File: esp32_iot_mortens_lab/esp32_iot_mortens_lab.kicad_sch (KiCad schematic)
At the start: 27 parts, among them J1 Conn_01x04, J2 Screw_Terminal_01x03, J3 Screw_Terminal_01x08, J4 Screw_Terminal_01x02, J5 USB_C_Receptacle_USB2.0_16P, K1 RT314A05, Q1 UMH3N, Q2 BC817, SW1 SW_Push, U1 ESP32-WROOM-32D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

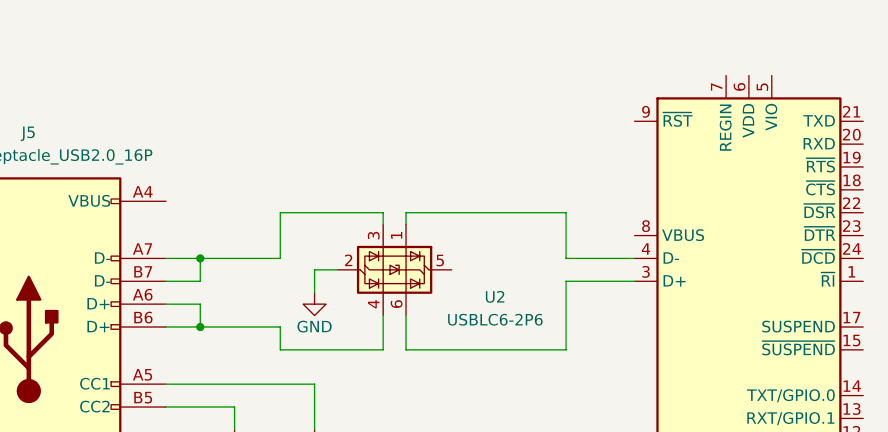
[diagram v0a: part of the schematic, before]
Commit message: upto adding power to the usb/uart circuit
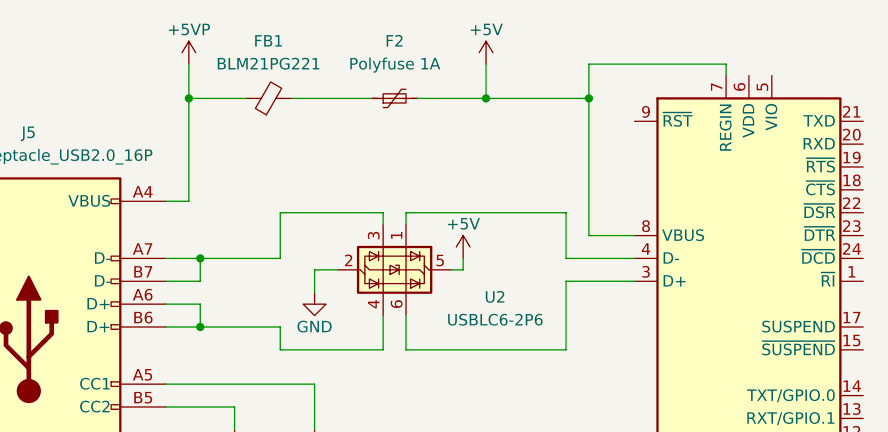
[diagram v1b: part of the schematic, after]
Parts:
- added F2: Polyfuse 1A, symbol Device:Polyfuse_Small
- added FB1: BLM21PG221, symbol Device:FerriteBead_Small
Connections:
- net +5V: now reaches U2.5 (VBUS)
- net +5V: now also U3.7 (REGIN), U3.8 (VBUS), F2.2
- net +5VP: now reaches J5.A4 (VBUS), J5.A9 (VBUS), J5.B4 (VBUS), J5.B9 (VBUS)
- net +5VP: now also FB1.1
- new net: F2.1, FB1.2

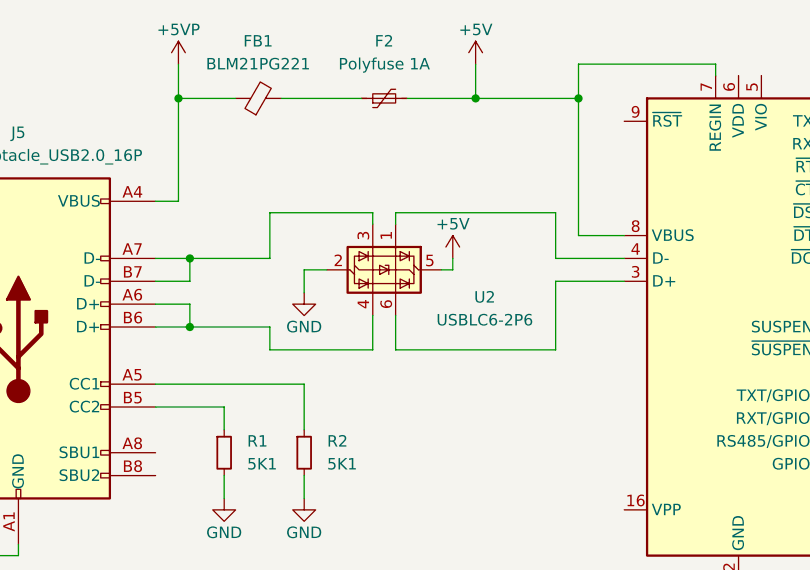
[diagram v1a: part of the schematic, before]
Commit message: pins 1,6 to D+; pins 3,4 to D- as per GPT and datasheet
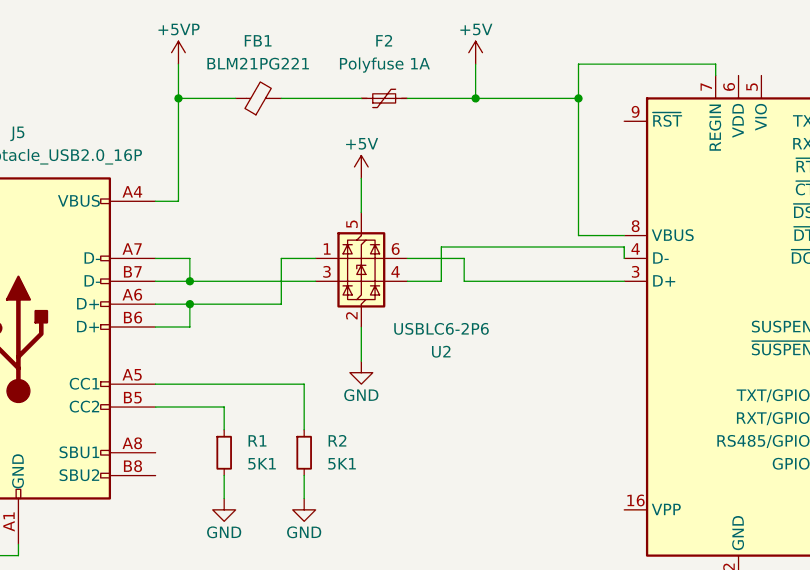
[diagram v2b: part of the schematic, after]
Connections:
- net at U2.1 (I/O1): now also J5.A6 (D+), J5.B6 (D+); no longer U3.4 (D-)
- new net: U2.4 (I/O2), U3.4 (D-)
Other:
- moved on the sheet: U2
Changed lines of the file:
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@@
+	)
+	(junction
+		(at 58.42 62.23)
+		(diameter 0)
+		(color 0 0 0 0)
 	)
 	(junction
@@
 	)
 	(junction
-		(at 101.6 41.91)
+		(at 58.42 64.77)
 		(diameter 0)
 		(color 0 0 0 0)
 	)
 	(junction
-		(at 58.42 67.31)
-		(diameter 0)
-		(color 0 0 0 0)
-	)
-	(junction
-		(at 58.42 59.69)
+		(at 101.6 41.91)
 		(diameter 0)
 		(color 0 0 0 0)
@@
 	(wire
 		(pts
-			(xy 71.12 60.96) (xy 73.66 60.96)
-		)
-		(stroke
-			(width 0)
-			(type default)
-		)
-	)
-	(wire
-		(pts
-			(xy 67.31 69.85) (xy 67.31 67.31)
+			(xy 82.55 62.23) (xy 86.36 62.23)
+		)
+		(stroke
+			(width 0)
+			(type default)
+		)
+	)
+	(wire
+		(pts
+			(xy 77.47 50.8) (xy 77.47 54.61)
 		)
 		(stroke
@@
 	(wire
 		(pts
-			(xy 81.28 54.61) (xy 99.06 54.61)
+			(xy 77.47 67.31) (xy 77.47 71.12)
 		)
 		(stroke
@@
 	(wire
 		(pts
-			(xy 99.06 62.23) (xy 106.68 62.23)
+			(xy 72.39 59.69) (xy 68.58 59.69)
 		)
 		(stroke
@@
 	(wire
 		(pts
+			(xy 88.9 62.23) (xy 106.68 62.23)
+		)
+		(stroke
+			(width 0)
+			(type default)
+		)
+	)
+	(wire
+		(pts
 			(xy 39.37 91.44) (xy 39.37 92.71)
 		)
@@
 	(wire
 		(pts
-			(xy 81.28 66.04) (xy 81.28 69.85)
-		)
-		(stroke
-			(width 0)
-			(type default)
-		)
-	)
-	(wire
-		(pts
 			(xy 57.15 38.1) (xy 57.15 41.91)
 		)
@@
 	(wire
 		(pts
-			(xy 67.31 69.85) (xy 78.74 69.85)
-		)
-		(stroke
-			(width 0)
-			(type default)
-		)
-	)
-	(wire
-		(pts
-			(xy 67.31 59.69) (xy 58.42 59.69)
+			(xy 68.58 59.69) (xy 68.58 64.77)
+		)
+		(stroke
+			(width 0)
+			(type default)
+		)
+	)
+	(wire
+		(pts
+			(xy 58.42 62.23) (xy 72.39 62.23)
 		)
 		(stroke
@@
 	(wire
 		(pts
-			(xy 81.28 55.88) (xy 81.28 54.61)
-		)
-		(stroke
-			(width 0)
-			(type default)
-		)
-	)
-	(wire
-		(pts
-			(xy 67.31 54.61) (xy 78.74 54.61)
+			(xy 88.9 59.69) (xy 88.9 62.23)
 		)
 		(stroke
@@
 	(wire
 		(pts
-			(xy 87.63 60.96) (xy 87.63 59.69)
-		)
-		(stroke
-			(width 0)
-			(type default)
-		)
-	)
-	(wire
-		(pts
 			(xy 101.6 38.1) (xy 116.84 38.1)
 		)
@@
 	(wire
 		(pts
-			(xy 78.74 54.61) (xy 78.74 55.88)
-		)
-		(stroke
-			(width 0)
-			(type default)
-		)
-	)
-	(wire
-		(pts
-			(xy 81.28 69.85) (xy 99.06 69.85)
-		)
-		(stroke
-			(width 0)
-			(type default)
-		)
-	)
-	(wire
-		(pts
-			(xy 67.31 59.69) (xy 67.31 54.61)
+			(xy 86.36 62.23) (xy 86.36 58.42)
 		)
 		(stroke
@@
 	(wire
 		(pts
-			(xy 58.42 67.31) (xy 58.42 64.77)
+			(xy 58.42 64.77) (xy 58.42 67.31)
 		)
 		(stroke
@@
 	(wire
 		(pts
-			(xy 78.74 66.04) (xy 78.74 69.85)
-		)
-		(stroke
-			(width 0)
-			(type default)
-		)
-	)
-	(wire
-		(pts
-			(xy 99.06 69.85) (xy 99.06 62.23)
-		)
-		(stroke
-			(width 0)
-			(type default)
-		)
-	)
-	(wire
-		(pts
-			(xy 86.36 60.96) (xy 87.63 60.96)
+			(xy 58.42 59.69) (xy 58.42 62.23)
 		)
 		(stroke
@@
 	(wire
 		(pts
-			(xy 67.31 67.31) (xy 58.42 67.31)
-		)
-		(stroke
-			(width 0)
-			(type default)
-		)
-	)
-	(wire
-		(pts
 			(xy 57.15 53.34) (xy 54.61 53.34)
 		)
@@
 	(wire
 		(pts
-			(xy 99.06 59.69) (xy 106.68 59.69)
-		)
-		(stroke
-			(width 0)
-			(type default)
-		)
-	)
-	(wire
-		(pts
 			(xy 54.61 64.77) (xy 58.42 64.77)
 		)
@@
 	(wire
 		(pts
-			(xy 71.12 63.5) (xy 71.12 60.96)
+			(xy 82.55 59.69) (xy 88.9 59.69)
 		)
 		(stroke
@@
 	(wire
 		(pts
-			(xy 99.06 54.61) (xy 99.06 59.69)
+			(xy 68.58 64.77) (xy 58.42 64.77)
+		)
+		(stroke
+			(width 0)
+			(type default)
+		)
+	)
+	(wire
+		(pts
+			(xy 86.36 58.42) (xy 106.68 58.42)
 		)
 		(stroke
@@
 	(wire
 		(pts
-			(xy 58.42 62.23) (xy 58.42 59.69)
+			(xy 106.68 58.42) (xy 106.68 59.69)
 		)
 		(stroke
@@
 	(symbol
 		(lib_id "Power_Protection:USBLC6-2P6")
-		(at 81.28 60.96 270)
+		(at 77.47 59.69 0)
 		(unit 1)
 		(exclude_from_sim no)
@@
 		(dnp no)
 		(property "Reference" "U2"
-			(at 91.186 64.008 90)
+			(at 86.36 70.104 0)
 			(effects
 				(font
@@
 		)
 		(property "Value" "USBLC6-2P6"
-			(at 91.186 66.548 90)
+			(at 86.36 67.564 0)
 			(effects
 				(font
@@
 		)
 		(property "Footprint" "Package_TO_SOT_SMD:SOT-666"
-			(at 74.549 61.976 0)
+			(at 78.486 66.421 0)
 			(effects
 				(font
@@
 		)
 		(property "Datasheet" "https://www.st.com/resource/en/datasheet/usblc6-2.pdf"
-			(at 72.644 61.976 0)
+			(at 78.486 68.326 0)
 			(effects
 				(font
@@
 		)
 		(property "Description" "Very low capacitance ESD protection diode, 2 data-line, SOT-666"
-			(at 81.28 60.96 0)
+			(at 77.47 59.69 0)
 			(effects
 				(font
@@
 	(symbol
 		(lib_id "power:+5V")
-		(at 87.63 59.69 0)
+		(at 77.47 50.8 0)
 		(unit 1)
 		(exclude_from_sim no)
@@
 		(dnp no)
 		(property "Reference" "#PWR07"
-			(at 87.63 63.5 0)
+			(at 77.47 54.61 0)
 			(effects
 				(font
@@
 		)
 		(property "Value" "+5V"
-			(at 87.63 55.88 0)
+			(at 77.47 46.99 0)
 			(effects
 				(font
@@
 		)
 		(property "Footprint" ""
-			(at 87.63 59.69 0)
+			(at 77.47 50.8 0)
 			(effects
 				(font
@@
 		)
 		(property "Datasheet" ""
-			(at 87.63 59.69 0)
+			(at 77.47 50.8 0)
 			(effects
 				(font
@@
 		)
 		(property "Description" "Power symbol creates a global label with name \"+5V\""
-			(at 87.63 59.69 0)
+			(at 77.47 50.8 0)
 			(effects
 				(font
@@
 	(symbol
 		(lib_id "power:GND")
-		(at 71.12 63.5 0)
+		(at 77.47 71.12 0)
 		(unit 1)
 		(exclude_from_sim no)
@@
 		(dnp no)
 		(property "Reference" "#PWR04"
-			(at 71.12 69.85 0)
+			(at 77.47 77.47 0)
 			(effects
 				(font
@@
 		)
 		(property "Value" "GND"
-			(at 71.12 67.31 0)
+			(at 77.47 74.93 0)
 			(effects
 				(font
@@
 		)
 		(property "Footprint" ""
-			(at 71.12 63.5 0)
+			(at 77.47 71.12 0)
 			(effects
 				(font
@@
 		)
 		(property "Datasheet" ""
-			(at 71.12 63.5 0)
+			(at 77.47 71.12 0)
 			(effects
 				(font
@@
 		)
 		(property "Description" "Power symbol creates a global label with name \"GND\" , ground"
-			(at 71.12 63.5 0)
-			(effects
-				(font
+			(at 77.47 71.12 0)
+			(effects
+				(font

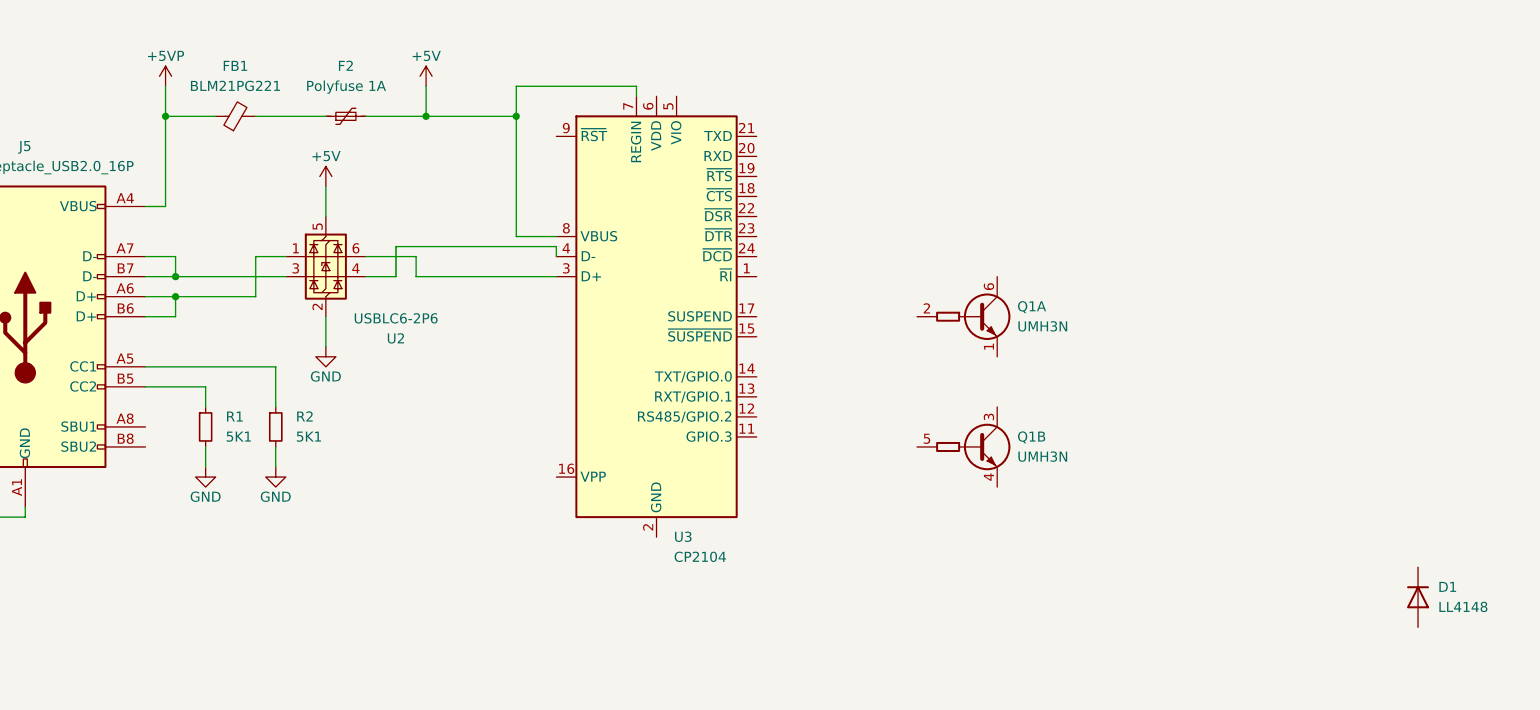
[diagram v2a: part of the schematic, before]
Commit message: added capacitors
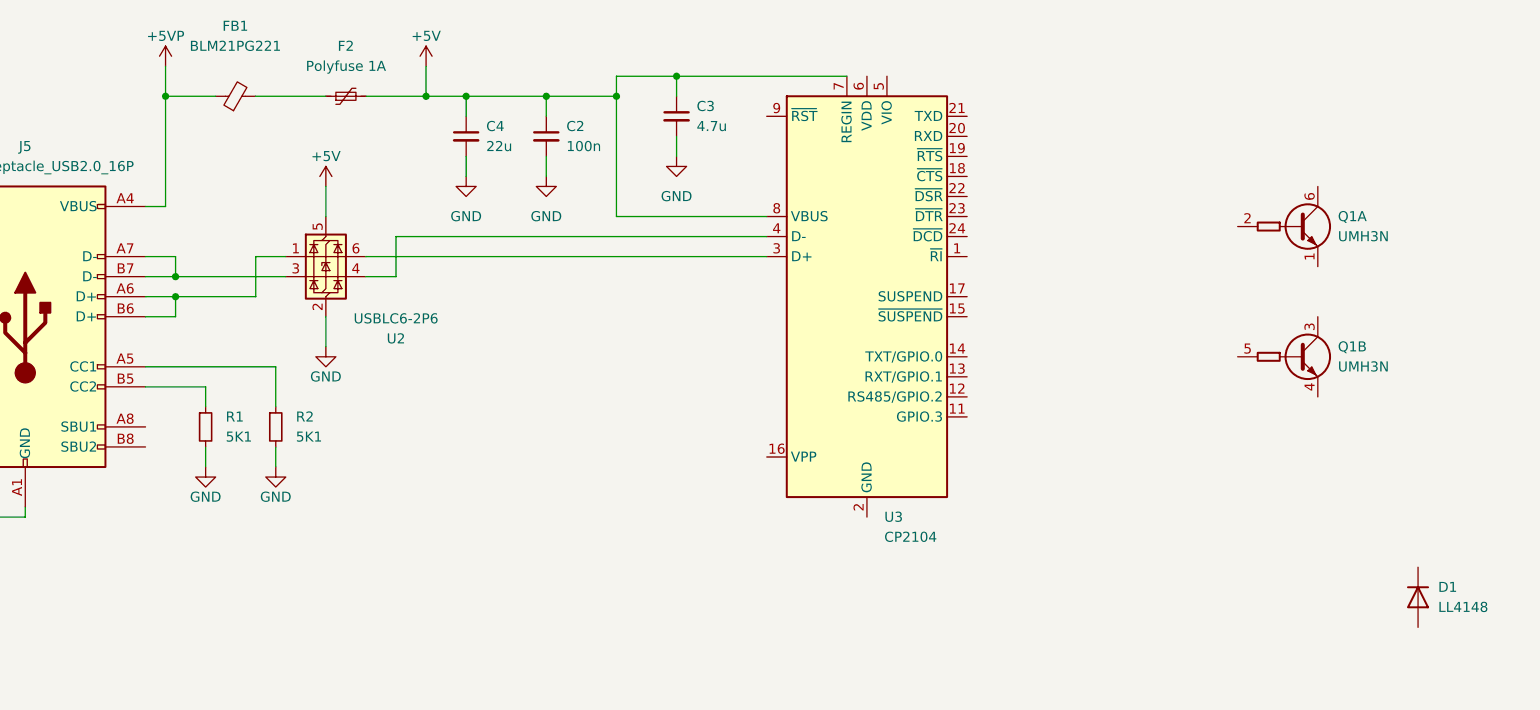
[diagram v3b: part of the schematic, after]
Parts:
- added C2: 100n, symbol Device:C_Small
- added C3: 4.7u, symbol Device:C_Small
- added C4: 22u, symbol Device:C_Small
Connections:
- net +5V: now also C2.1, C3.1, C4.1
- net GND: now also C2.2, C3.2, C4.2
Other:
- moved on the sheet: F2, FB1, Q1A, Q1B, U3

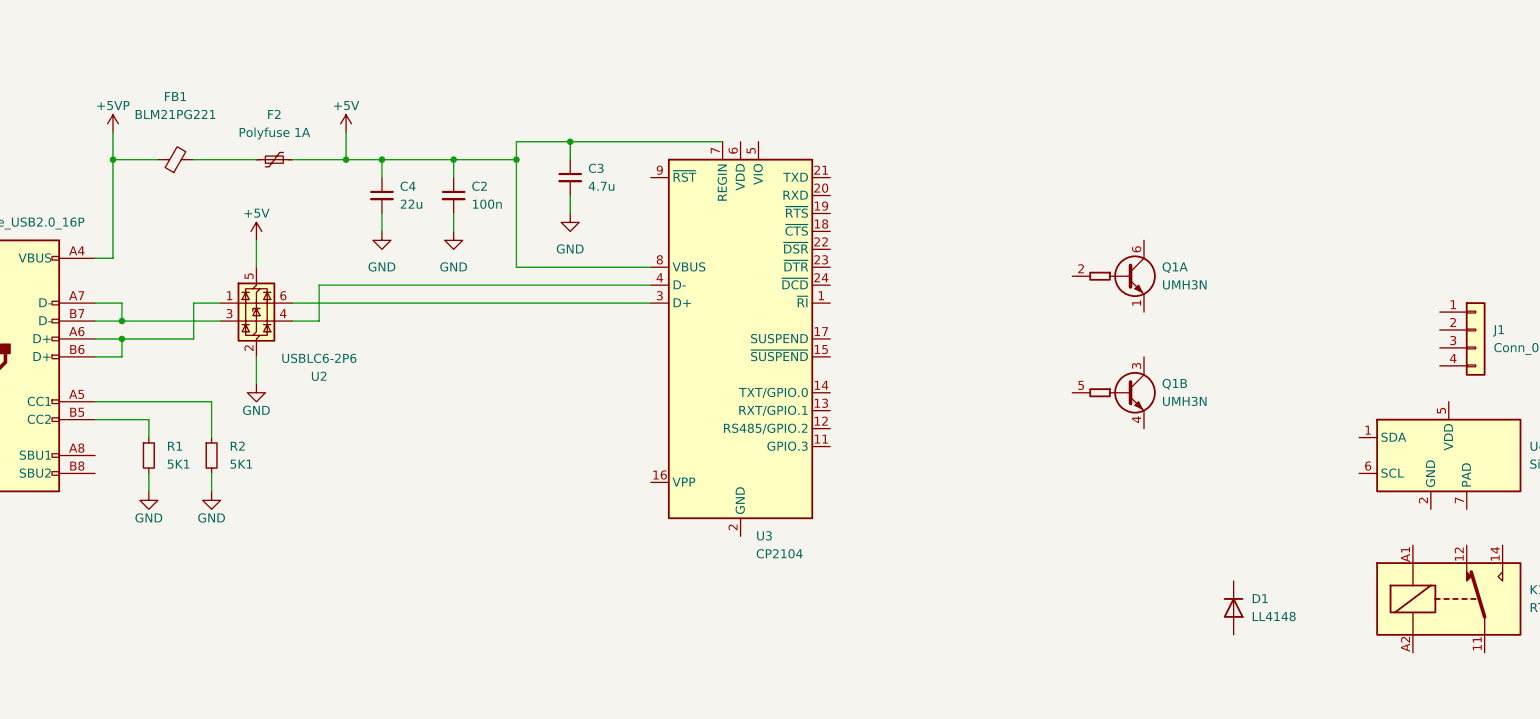
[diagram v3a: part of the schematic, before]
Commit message: upto VDD/VIO/VPP pins
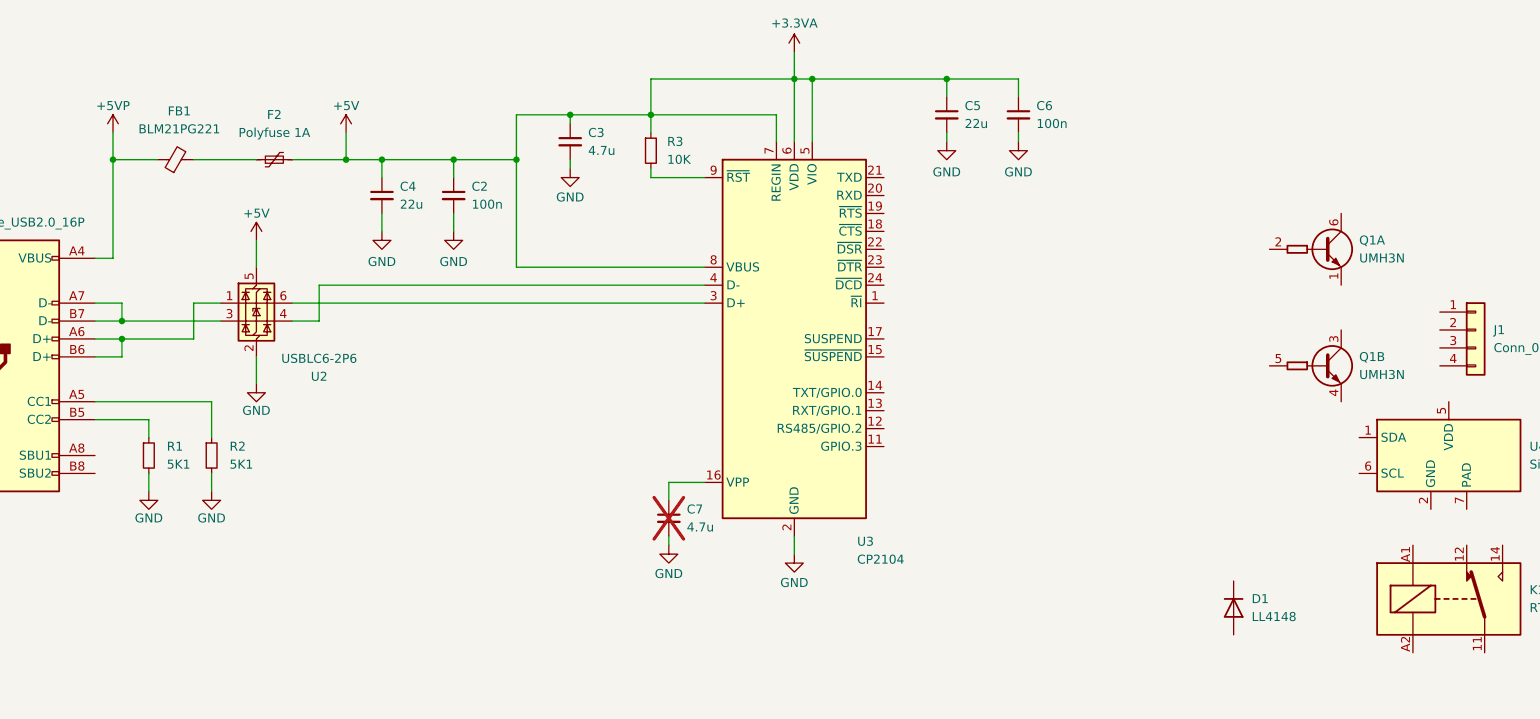
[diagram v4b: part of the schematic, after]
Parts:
- added C5: 22u, symbol Device:C_Small
- added C6: 100n, symbol Device:C_Small
- added C7: 4.7u, symbol Device:C_Small
- added R3: 10K, symbol Device:R_Small
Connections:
- net +5V is gone; now on net +3.3VA: C2.1, C3.1, C4.1, F2.2, U2.5 (VBUS), U3.7 (REGIN), U3.8 (VBUS)
- net GND: now also U3.2 (GND), U3.25 (GND), C5.2, C6.2, C7.2
- net at U3.16 (VPP): now also C7.1
- net +3.3VA: now reaches U3.5 (VIO)
- net +3.3VA: now also U3.6 (VDD), C5.1, C6.1, R3.1
- net at U3.9 (~{RST}): now also R3.2
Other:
- moved on the sheet: C3, Q1A, Q1B, U3

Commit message: RTS/DTR subcircuit
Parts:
- added R4, R5: 22R, symbol Device:R_Small
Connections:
- net DTR: now reaches Q1.1 (E1)
- net DTR: now also Q1.5 (B2), U3.23 (~{DTR})
- net RTS: now reaches Q1.2 (B1)
- net RTS: now also Q1.3 (C2), U3.19 (~{RTS})
- net IO0: now reaches Q1.6 (C1)
- net at U3.20 (RXD): now also R5.1
- net at U3.21 (TXD): now also R4.1
- net EN: now reaches Q1.4 (E2)
- new net RX: R4.2
- new net TX: R5.2
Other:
- moved on the sheet: C5, C6, Q1A, Q1B
